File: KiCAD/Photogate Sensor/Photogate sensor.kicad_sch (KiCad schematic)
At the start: 14 parts, among them J1 Conn_01x03_Pin, J2 Conn_01x03_Pin, Q1 Q_NMOS_GDS, U1 MCP6541

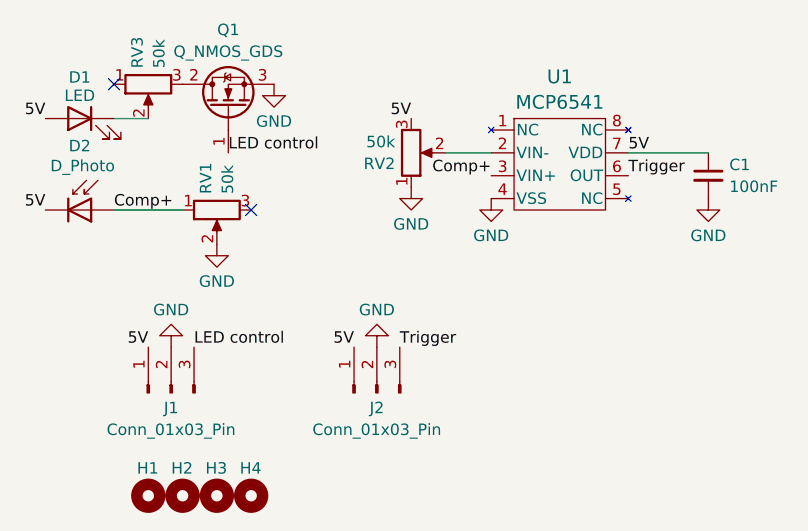
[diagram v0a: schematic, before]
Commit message: Add status LED, improve traces
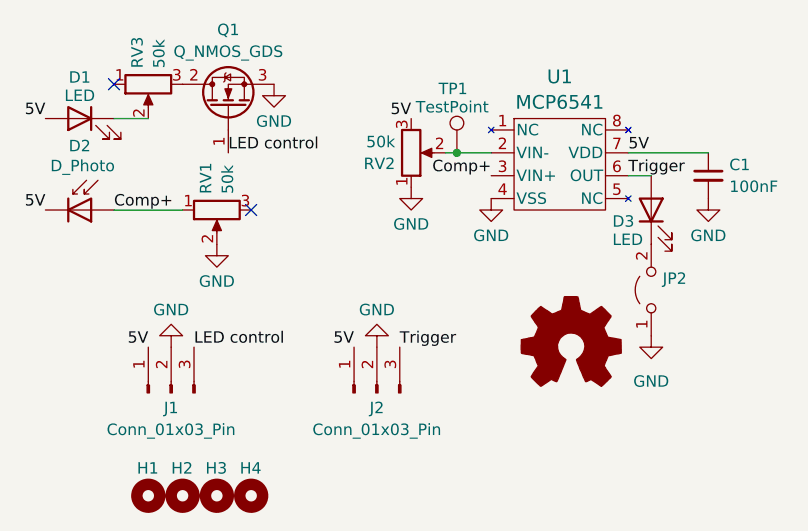
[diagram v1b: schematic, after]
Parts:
- added D3: LED, LED_THT:LED_D3.0mm, symbol Device:LED
- added JP2: Jumper_2_Open, Jumper:SolderJumper-2_P1.3mm_Open_RoundedPad1.0x1.5mm, symbol Jumper:Jumper_2_Open
- added SYM1: Logo_Open_Hardware_Small, Custom:CC-BY-SA Symbol, symbol Graphic:Logo_Open_Hardware_Small
- added TP1: TestPoint, TestPoint:TestPoint_Pad_D1.0mm, symbol Connector:TestPoint
- H1, H2, H3, H4: footprint MountingHole:MountingHole_4.3mm_M4 -> Custom:MountingHole_4.3mm_M4
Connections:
- net GND: now also JP2.1 (A)
- net Trigger: now also D3.2 (A)
- net at RV2.2, U1.2 (VIN-): now also TP1.1
- new net: D3.1 (K), JP2.2 (B)

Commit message: Update trimpot values
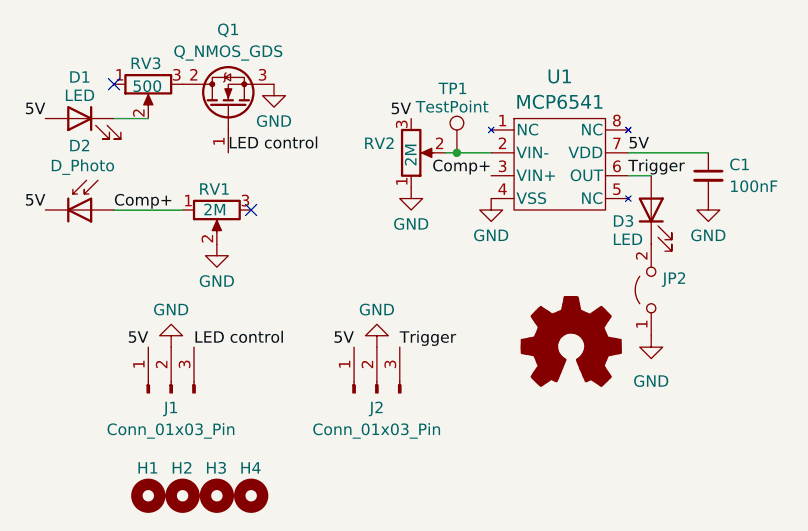
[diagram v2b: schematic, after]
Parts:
- RV1, RV2: value 50k -> 2M; Part PV36W503C01B00 -> PV36W205C01B00
- RV3: value 50k -> 500; Part PV36W503C01B00 -> PV36W501C01B00
